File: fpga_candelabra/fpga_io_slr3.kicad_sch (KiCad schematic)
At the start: 12 parts, among them U1 XCVU13P-B2104

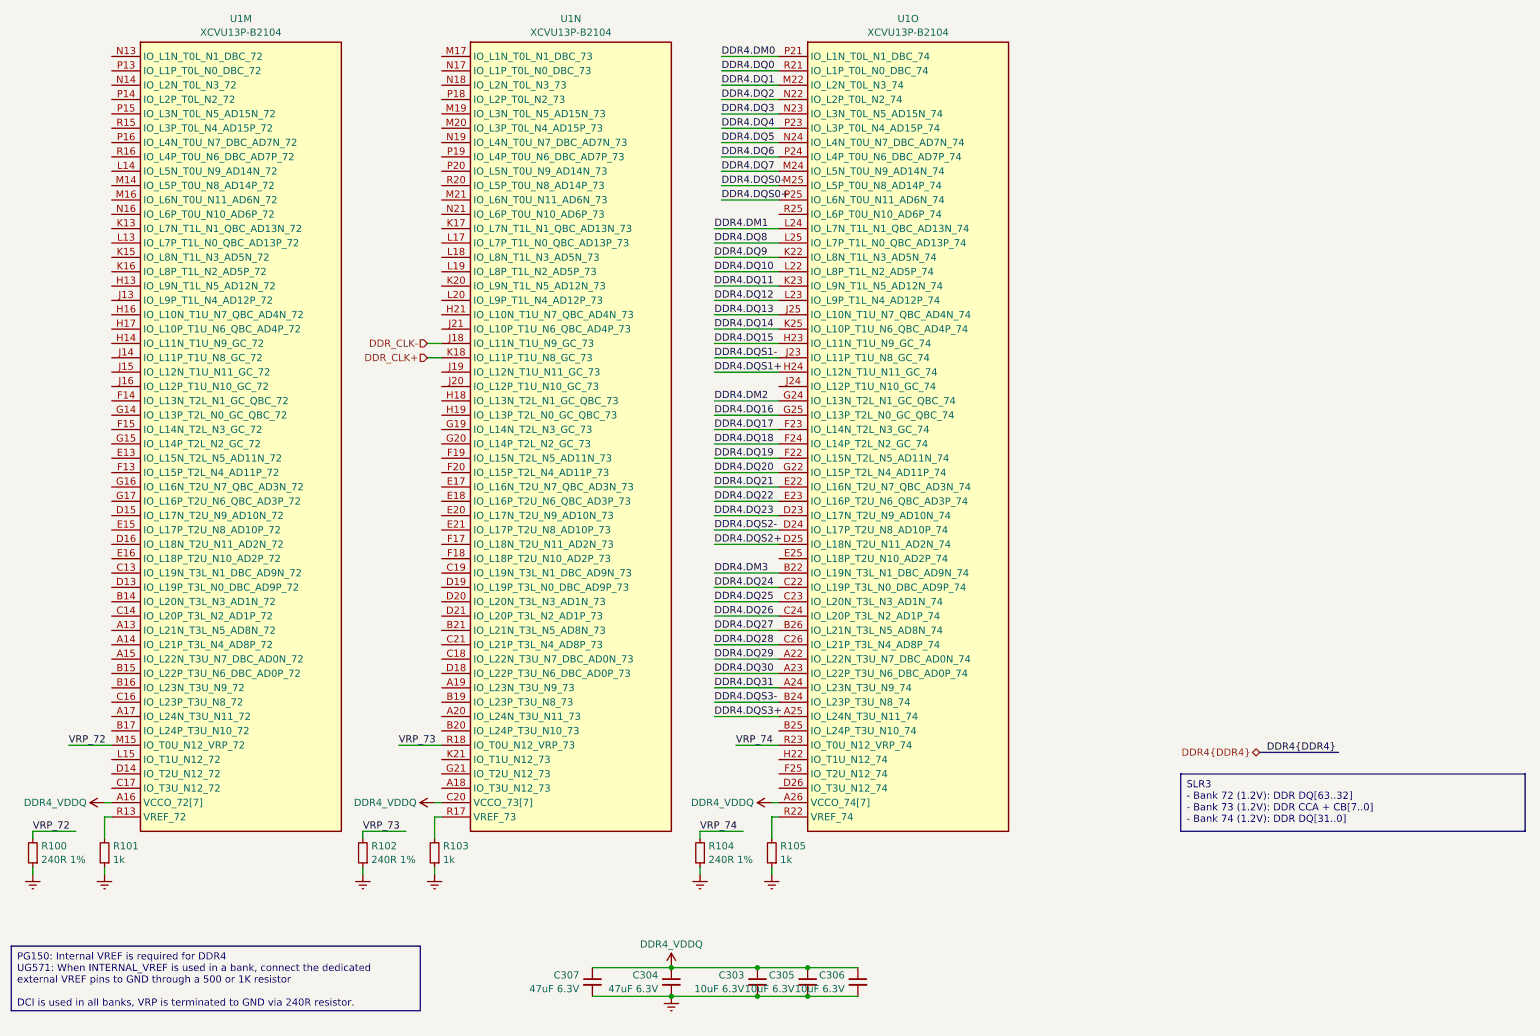
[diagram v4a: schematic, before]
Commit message: fpga_candelabra: major revision
* Finish DDR4 & QSFP+ & PCIe layout
* Change FMC to LPC
* Add mikroBUS extension
* 12V input & PDN updates
* FPGA config updates

Signed-off-by: Yichuan Gao <gaoyichuan000@gmail.com>
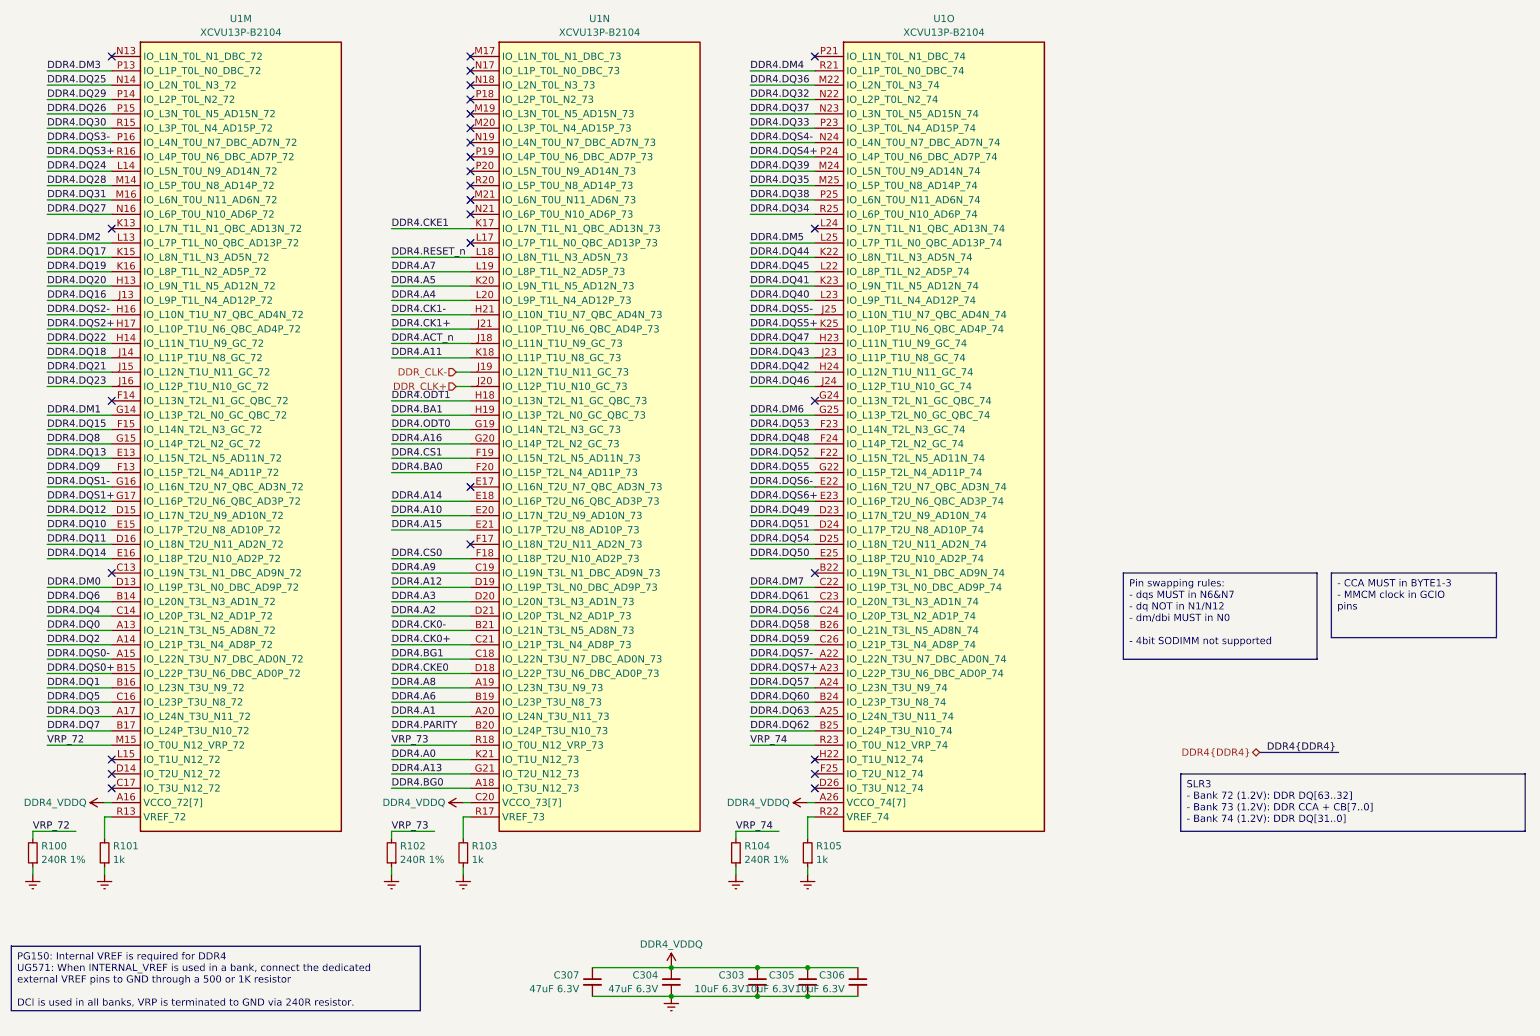
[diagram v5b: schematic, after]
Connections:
- net DDR4.DM0: now also U1.D13 (IO_L19P_T3L_N0_DBC_AD9P_72); no longer U1.P21 (IO_L1N_T0L_N1_DBC_74)
- net DDR4.DM1: now also U1.G14 (IO_L13P_T2L_N0_GC_QBC_72); no longer U1.L24 (IO_L7N_T1L_N1_QBC_AD13N_74)
- net DDR4.DM2: now also U1.L13 (IO_L7P_T1L_N0_QBC_AD13P_72); no longer U1.G24 (IO_L13N_T2L_N1_GC_QBC_74)
- net DDR4.DM3: now also U1.P13 (IO_L1P_T0L_N0_DBC_72); no longer U1.B22 (IO_L19N_T3L_N1_DBC_AD9N_74)
- net DDR4.DQ0: now also U1.A13 (IO_L21N_T3L_N5_AD8N_72); no longer U1.R21 (IO_L1P_T0L_N0_DBC_74)
- net DDR4.DQ1: now also U1.B16 (IO_L23N_T3U_N9_72); no longer U1.M22 (IO_L2N_T0L_N3_74)
- net DDR4.DQ10: now also U1.E15 (IO_L17P_T2U_N8_AD10P_72); no longer U1.L22 (IO_L8P_T1L_N2_AD5P_74)
- net DDR4.DQ11: now also U1.D16 (IO_L18N_T2U_N11_AD2N_72); no longer U1.K23 (IO_L9N_T1L_N5_AD12N_74)
- net DDR4.DQ12: now also U1.D15 (IO_L17N_T2U_N9_AD10N_72); no longer U1.L23 (IO_L9P_T1L_N4_AD12P_74)
- net DDR4.DQ13: now also U1.E13 (IO_L15N_T2L_N5_AD11N_72); no longer U1.J25 (IO_L10N_T1U_N7_QBC_AD4N_74)
- net DDR4.DQ14: now also U1.E16 (IO_L18P_T2U_N10_AD2P_72); no longer U1.K25 (IO_L10P_T1U_N6_QBC_AD4P_74)
- net DDR4.DQ15: now also U1.F15 (IO_L14N_T2L_N3_GC_72); no longer U1.H23 (IO_L11N_T1U_N9_GC_74)
- net DDR4.DQ16: now also U1.J13 (IO_L9P_T1L_N4_AD12P_72); no longer U1.G25 (IO_L13P_T2L_N0_GC_QBC_74)
- net DDR4.DQ17: now also U1.K15 (IO_L8N_T1L_N3_AD5N_72); no longer U1.F23 (IO_L14N_T2L_N3_GC_74)
- net DDR4.DQ18: now also U1.J14 (IO_L11P_T1U_N8_GC_72); no longer U1.F24 (IO_L14P_T2L_N2_GC_74)
- net DDR4.DQ19: now also U1.K16 (IO_L8P_T1L_N2_AD5P_72); no longer U1.F22 (IO_L15N_T2L_N5_AD11N_74)
- net DDR4.DQ2: now also U1.A14 (IO_L21P_T3L_N4_AD8P_72); no longer U1.N22 (IO_L2P_T0L_N2_74)
- net DDR4.DQ20: now also U1.H13 (IO_L9N_T1L_N5_AD12N_72); no longer U1.G22 (IO_L15P_T2L_N4_AD11P_74)
- net DDR4.DQ21: now also U1.J15 (IO_L12N_T1U_N11_GC_72); no longer U1.E22 (IO_L16N_T2U_N7_QBC_AD3N_74)
- net DDR4.DQ22: now also U1.H14 (IO_L11N_T1U_N9_GC_72); no longer U1.E23 (IO_L16P_T2U_N6_QBC_AD3P_74)
- net DDR4.DQ23: now also U1.J16 (IO_L12P_T1U_N10_GC_72); no longer U1.D23 (IO_L17N_T2U_N9_AD10N_74)
- net DDR4.DQ24: now also U1.L14 (IO_L5N_T0U_N9_AD14N_72); no longer U1.C22 (IO_L19P_T3L_N0_DBC_AD9P_74)
- net DDR4.DQ25: now also U1.N14 (IO_L2N_T0L_N3_72); no longer U1.C23 (IO_L20N_T3L_N3_AD1N_74)
- net DDR4.DQ26: now also U1.P15 (IO_L3N_T0L_N5_AD15N_72); no longer U1.C24 (IO_L20P_T3L_N2_AD1P_74)
- net DDR4.DQ27: now also U1.N16 (IO_L6P_T0U_N10_AD6P_72); no longer U1.B26 (IO_L21N_T3L_N5_AD8N_74)
- net DDR4.DQ28: now also U1.M14 (IO_L5P_T0U_N8_AD14P_72); no longer U1.C26 (IO_L21P_T3L_N4_AD8P_74)
- net DDR4.DQ29: now also U1.P14 (IO_L2P_T0L_N2_72); no longer U1.A22 (IO_L22N_T3U_N7_DBC_AD0N_74)
- net DDR4.DQ3: now also U1.A17 (IO_L24N_T3U_N11_72); no longer U1.N23 (IO_L3N_T0L_N5_AD15N_74)
- net DDR4.DQ30: now also U1.R15 (IO_L3P_T0L_N4_AD15P_72); no longer U1.A23 (IO_L22P_T3U_N6_DBC_AD0P_74)
- net DDR4.DQ31: now also U1.M16 (IO_L6N_T0U_N11_AD6N_72); no longer U1.A24 (IO_L23N_T3U_N9_74)
- net DDR4.DQ4: now also U1.C14 (IO_L20P_T3L_N2_AD1P_72); no longer U1.P23 (IO_L3P_T0L_N4_AD15P_74)
- net DDR4.DQ5: now also U1.C16 (IO_L23P_T3U_N8_72); no longer U1.N24 (IO_L4N_T0U_N7_DBC_AD7N_74)
- net DDR4.DQ6: now also U1.B14 (IO_L20N_T3L_N3_AD1N_72); no longer U1.P24 (IO_L4P_T0U_N6_DBC_AD7P_74)
- net DDR4.DQ7: now also U1.B17 (IO_L24P_T3U_N10_72); no longer U1.M24 (IO_L5N_T0U_N9_AD14N_74)
- net DDR4.DQ8: now also U1.G15 (IO_L14P_T2L_N2_GC_72); no longer U1.L25 (IO_L7P_T1L_N0_QBC_AD13P_74)
- net DDR4.DQ9: now also U1.F13 (IO_L15P_T2L_N4_AD11P_72); no longer U1.K22 (IO_L8N_T1L_N3_AD5N_74)
- net DDR4.DQS0+: now also U1.B15 (IO_L22P_T3U_N6_DBC_AD0P_72); no longer U1.P25 (IO_L6N_T0U_N11_AD6N_74)
- net DDR4.DQS0-: now also U1.A15 (IO_L22N_T3U_N7_DBC_AD0N_72); no longer U1.M25 (IO_L5P_T0U_N8_AD14P_74)
- net DDR4.DQS1+: now also U1.G17 (IO_L16P_T2U_N6_QBC_AD3P_72); no longer U1.H24 (IO_L12N_T1U_N11_GC_74)
- net DDR4.DQS1-: now also U1.G16 (IO_L16N_T2U_N7_QBC_AD3N_72); no longer U1.J23 (IO_L11P_T1U_N8_GC_74)
- net DDR4.DQS2+: now also U1.H17 (IO_L10P_T1U_N6_QBC_AD4P_72); no longer U1.D25 (IO_L18N_T2U_N11_AD2N_74)
- net DDR4.DQS2-: now also U1.H16 (IO_L10N_T1U_N7_QBC_AD4N_72); no longer U1.D24 (IO_L17P_T2U_N8_AD10P_74)
- net DDR4.DQS3+: now also U1.R16 (IO_L4P_T0U_N6_DBC_AD7P_72); no longer U1.A25 (IO_L24N_T3U_N11_74)
- net DDR4.DQS3-: now also U1.P16 (IO_L4N_T0U_N7_DBC_AD7N_72); no longer U1.B24 (IO_L23P_T3U_N8_74)
- net DDR_CLK+: now also U1.J20 (IO_L12P_T1U_N10_GC_73); no longer U1.K18 (IO_L11P_T1U_N8_GC_73)
- net DDR_CLK-: now also U1.J19 (IO_L12N_T1U_N11_GC_73); no longer U1.J18 (IO_L11N_T1U_N9_GC_73)
- net DDR4.DQ62: now reaches U1.B25 (IO_L24P_T3U_N10_74)
- net DDR4.DQ50: now reaches U1.E25 (IO_L18P_T2U_N10_AD2P_74)
- net DDR4.DQ46: now reaches U1.J24 (IO_L12P_T1U_N10_GC_74)
- net DDR4.DQ34: now reaches U1.R25 (IO_L6P_T0U_N10_AD6P_74)
- net DDR4.BG0: now reaches U1.A18 (IO_T3U_N12_73)
- net DDR4.A8: now reaches U1.A19 (IO_L23N_T3U_N9_73)
- net DDR4.A1: now reaches U1.A20 (IO_L24N_T3U_N11_73)
- net DDR4.A6: now reaches U1.B19 (IO_L23P_T3U_N8_73)
- net DDR4.PARITY: now reaches U1.B20 (IO_L24P_T3U_N10_73)
- net DDR4.CK0-: now reaches U1.B21 (IO_L21N_T3L_N5_AD8N_73)
- net DDR4.BG1: now reaches U1.C18 (IO_L22N_T3U_N7_DBC_AD0N_73)
- net DDR4.A9: now reaches U1.C19 (IO_L19N_T3L_N1_DBC_AD9N_73)
- net DDR4.CK0+: now reaches U1.C21 (IO_L21P_T3L_N4_AD8P_73)
- net DDR4.CKE0: now reaches U1.D18 (IO_L22P_T3U_N6_DBC_AD0P_73)
- net DDR4.A12: now reaches U1.D19 (IO_L19P_T3L_N0_DBC_AD9P_73)
- net DDR4.A3: now reaches U1.D20 (IO_L20N_T3L_N3_AD1N_73)
- net DDR4.A2: now reaches U1.D21 (IO_L20P_T3L_N2_AD1P_73)
- net DDR4.A14: now reaches U1.E18 (IO_L16P_T2U_N6_QBC_AD3P_73)
- net DDR4.A10: now reaches U1.E20 (IO_L17N_T2U_N9_AD10N_73)
- net DDR4.A15: now reaches U1.E21 (IO_L17P_T2U_N8_AD10P_73)
- net DDR4.CS0: now reaches U1.F18 (IO_L18P_T2U_N10_AD2P_73)
- net DDR4.CS1: now reaches U1.F19 (IO_L15N_T2L_N5_AD11N_73)
- net DDR4.BA0: now reaches U1.F20 (IO_L15P_T2L_N4_AD11P_73)
- net DDR4.ODT0: now reaches U1.G19 (IO_L14N_T2L_N3_GC_73)
- net DDR4.A16: now reaches U1.G20 (IO_L14P_T2L_N2_GC_73)
- net DDR4.A13: now reaches U1.G21 (IO_T2U_N12_73)
- net DDR4.ODT1: now reaches U1.H18 (IO_L13N_T2L_N1_GC_QBC_73)
- net DDR4.BA1: now reaches U1.H19 (IO_L13P_T2L_N0_GC_QBC_73)
- net DDR4.CK1-: now reaches U1.H21 (IO_L10N_T1U_N7_QBC_AD4N_73)
- net DDR4.CK1+: now reaches U1.J21 (IO_L10P_T1U_N6_QBC_AD4P_73)
- net DDR4.CKE1: now reaches U1.K17 (IO_L7N_T1L_N1_QBC_AD13N_73)
- net DDR4.A5: now reaches U1.K20 (IO_L9N_T1L_N5_AD12N_73)
- net DDR4.A0: now reaches U1.K21 (IO_T1U_N12_73)
- net DDR4.RESET_n: now reaches U1.L18 (IO_L8N_T1L_N3_AD5N_73)
- net DDR4.A7: now reaches U1.L19 (IO_L8P_T1L_N2_AD5P_73)
- net DDR4.A4: now reaches U1.L20 (IO_L9P_T1L_N4_AD12P_73)
- new net DDR4.A11: U1.K18 (IO_L11P_T1U_N8_GC_73)
- new net DDR4.ACT_n: U1.J18 (IO_L11N_T1U_N9_GC_73)
- new net DDR4.DM4: U1.R21 (IO_L1P_T0L_N0_DBC_74)
- new net DDR4.DM5: U1.L25 (IO_L7P_T1L_N0_QBC_AD13P_74)
- new net DDR4.DM6: U1.G25 (IO_L13P_T2L_N0_GC_QBC_74)
- new net DDR4.DM7: U1.C22 (IO_L19P_T3L_N0_DBC_AD9P_74)
- new net DDR4.DQ32: U1.N22 (IO_L2P_T0L_N2_74)
- new net DDR4.DQ33: U1.P23 (IO_L3P_T0L_N4_AD15P_74)
- new net DDR4.DQ35: U1.M25 (IO_L5P_T0U_N8_AD14P_74)
- new net DDR4.DQ36: U1.M22 (IO_L2N_T0L_N3_74)
- new net DDR4.DQ37: U1.N23 (IO_L3N_T0L_N5_AD15N_74)
- new net DDR4.DQ38: U1.P25 (IO_L6N_T0U_N11_AD6N_74)
- new net DDR4.DQ39: U1.M24 (IO_L5N_T0U_N9_AD14N_74)
- new net DDR4.DQ40: U1.L23 (IO_L9P_T1L_N4_AD12P_74)
- new net DDR4.DQ41: U1.K23 (IO_L9N_T1L_N5_AD12N_74)
- new net DDR4.DQ42: U1.H24 (IO_L12N_T1U_N11_GC_74)
- new net DDR4.DQ43: U1.J23 (IO_L11P_T1U_N8_GC_74)
- new net DDR4.DQ44: U1.K22 (IO_L8N_T1L_N3_AD5N_74)
- new net DDR4.DQ45: U1.L22 (IO_L8P_T1L_N2_AD5P_74)
- new net DDR4.DQ47: U1.H23 (IO_L11N_T1U_N9_GC_74)
- new net DDR4.DQ48: U1.F24 (IO_L14P_T2L_N2_GC_74)
- new net DDR4.DQ49: U1.D23 (IO_L17N_T2U_N9_AD10N_74)
- new net DDR4.DQ51: U1.D24 (IO_L17P_T2U_N8_AD10P_74)
- new net DDR4.DQ52: U1.F22 (IO_L15N_T2L_N5_AD11N_74)
- new net DDR4.DQ53: U1.F23 (IO_L14N_T2L_N3_GC_74)
- new net DDR4.DQ54: U1.D25 (IO_L18N_T2U_N11_AD2N_74)
- new net DDR4.DQ55: U1.G22 (IO_L15P_T2L_N4_AD11P_74)
- new net DDR4.DQ56: U1.C24 (IO_L20P_T3L_N2_AD1P_74)
- new net DDR4.DQ57: U1.A24 (IO_L23N_T3U_N9_74)
- new net DDR4.DQ58: U1.B26 (IO_L21N_T3L_N5_AD8N_74)
- new net DDR4.DQ59: U1.C26 (IO_L21P_T3L_N4_AD8P_74)
- new net DDR4.DQ60: U1.B24 (IO_L23P_T3U_N8_74)
- new net DDR4.DQ61: U1.C23 (IO_L20N_T3L_N3_AD1N_74)
- new net DDR4.DQ63: U1.A25 (IO_L24N_T3U_N11_74)
- new net DDR4.DQS4+: U1.P24 (IO_L4P_T0U_N6_DBC_AD7P_74)
- new net DDR4.DQS4-: U1.N24 (IO_L4N_T0U_N7_DBC_AD7N_74)
- new net DDR4.DQS5+: U1.K25 (IO_L10P_T1U_N6_QBC_AD4P_74)
- new net DDR4.DQS5-: U1.J25 (IO_L10N_T1U_N7_QBC_AD4N_74)
- new net DDR4.DQS6+: U1.E23 (IO_L16P_T2U_N6_QBC_AD3P_74)
- new net DDR4.DQS6-: U1.E22 (IO_L16N_T2U_N7_QBC_AD3N_74)
- new net DDR4.DQS7+: U1.A23 (IO_L22P_T3U_N6_DBC_AD0P_74)
- new net DDR4.DQS7-: U1.A22 (IO_L22N_T3U_N7_DBC_AD0N_74)
- no-connect marks 0 -> 29
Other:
- moved on the sheet: R102, R103, R104, R105, U1N, U1O

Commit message: fpga_candelabra: add author & rev to schematics
Signed-off-by: Yichuan Gao <gaoyichuan000@gmail.com>
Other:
- company: (none) -> CHIPS Alliance
- title: (none) -> FPGA SLR3 IO
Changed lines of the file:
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@@
 	(generator_version "8.0")
 	(paper "A4")
+	(title_block
+		(title "FPGA SLR3 IO")
+		(date "2025-02-05")
+		(rev "0.2.0")
+		(company "CHIPS Alliance")
+		(comment 1 "Yichuan Gao")
+		(comment 2 "Yichuan Gao")
+	)
 	(junction
 		(at 156.21 190.5)
